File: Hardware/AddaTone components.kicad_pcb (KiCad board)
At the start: 2 copper layers, 60 x 110 mm, 95 parts, among them J1 SWD_Header, J2 Conn_01x10_Female, J3 Conn_01x12_Female, J4 Conn_01x03_Male, J5 Conn_01x06_Male, J6 Conn_01x03_Male, J7 Conn_01x02_Male, J8 Eurorack_16_pin_power, U1 STM32F446RETx, U2 ICE40UP5K-SG48ITR, U3 MCP6004, U4 PCM5100APW, U5 TL072, U6 LD1117S12TR, U7 LM1117-3.3, Y1 ECS-12MHz

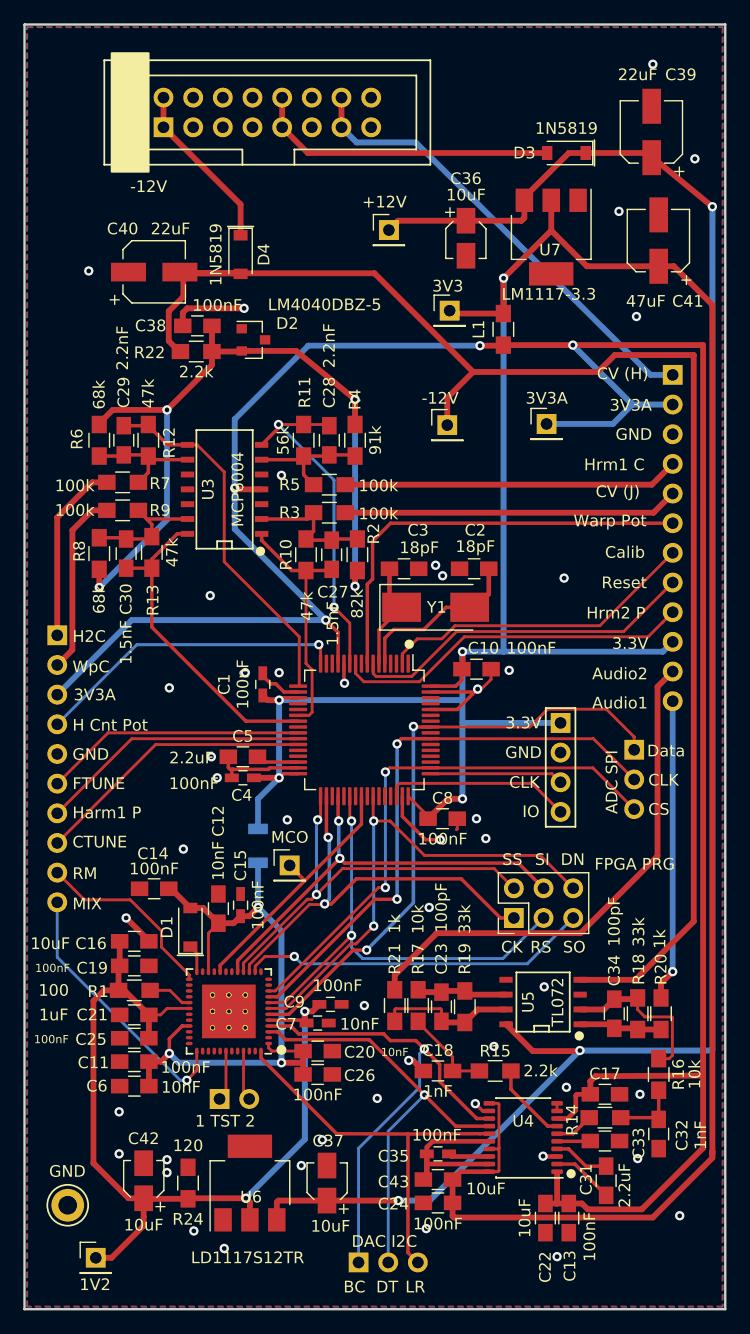
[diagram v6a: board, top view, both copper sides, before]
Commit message: Updating component schematic and PCB to Kicad 7.09
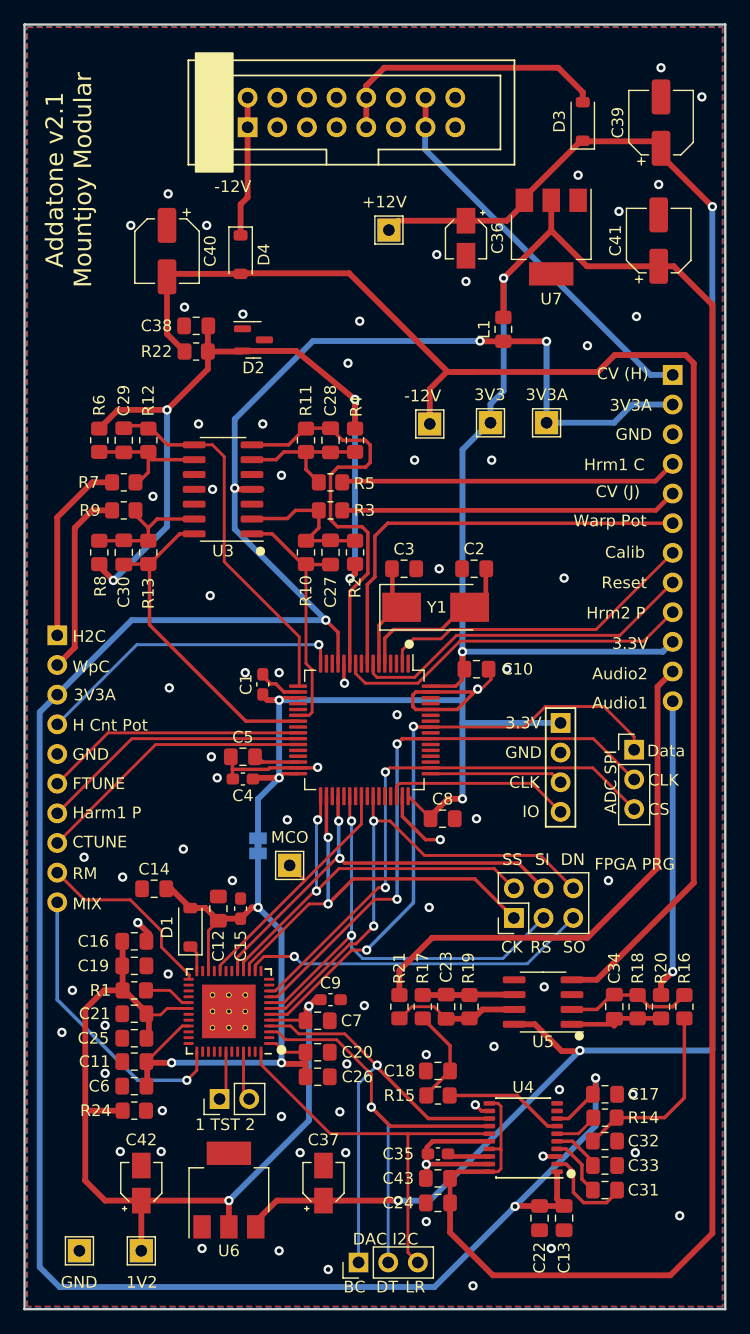
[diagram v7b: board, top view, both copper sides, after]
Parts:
- C1, C15, C35, C4, C9: footprint Capacitors_SMD:C_0603_HandSoldering -> Capacitor_SMD:C_0603_1608Metric_Pad1.08x0.95mm_HandSolder
- C10, C11, C12, C13, C14, C16, C17, C18, C19, C20, C21, C22, C23, C24, C25, C26, C27, C28, C29, C30, C31, C32, C33, C34, C38, C43, C5, C6, C8: footprint Capacitors_SMD:C_0805_HandSoldering -> Capacitor_SMD:C_0805_2012Metric_Pad1.18x1.45mm_HandSolder
- C2, C3: value 18pF -> 30pF; footprint Capacitors_SMD:C_0805_HandSoldering -> Capacitor_SMD:C_0805_2012Metric_Pad1.18x1.45mm_HandSolder
- C36, C37, C42: footprint Capacitors_SMD:CP_Elec_3x5.3 -> Capacitor_SMD:CP_Elec_3x5.3
- C39, C40, C41: footprint Capacitors_SMD:CP_Elec_5x5.3 -> Capacitor_SMD:CP_Elec_5x5.3
- C7: footprint Capacitors_SMD:C_0603_HandSoldering -> Capacitor_SMD:C_0805_2012Metric_Pad1.18x1.45mm_HandSolder
- D1, D3, D4: footprint Diodes_SMD:D_SOD-123 -> Diode_SMD:D_SOD-123
- D2: footprint TO_SOT_Packages_SMD:SOT-23 -> Package_TO_SOT_SMD:SOT-23
- J2: footprint Socket_Strips:Socket_Strip_Straight_1x10_Pitch2.54mm -> Connector_PinSocket_2.54mm:PinSocket_1x10_P2.54mm_Vertical
- J3: footprint Socket_Strips:Socket_Strip_Straight_1x12_Pitch2.54mm -> Connector_PinSocket_2.54mm:PinSocket_1x12_P2.54mm_Vertical
- J4, J6: footprint Pin_Headers:Pin_Header_Straight_1x03_Pitch2.54mm -> Connector_PinHeader_2.54mm:PinHeader_1x03_P2.54mm_Vertical
- J5: footprint Pin_Headers:Pin_Header_Straight_2x03_Pitch2.54mm -> Connector_PinHeader_2.54mm:PinHeader_2x03_P2.54mm_Vertical
- J7: footprint Pin_Headers:Pin_Header_Straight_1x02_Pitch2.54mm -> Connector_PinHeader_2.54mm:PinHeader_1x02_P2.54mm_Vertical
- L1: footprint Inductors_SMD:L_0805_HandSoldering -> Inductor_SMD:L_0805_2012Metric_Pad1.15x1.40mm_HandSolder
- R1, R10, R11, R12, R13, R14, R15, R16, R17, R18, R19, R2, R20, R21, R22, R24, R3, R4, R5, R6, R7, R8, R9: footprint Resistors_SMD:R_0805_HandSoldering -> Resistor_SMD:R_0805_2012Metric_Pad1.20x1.40mm_HandSolder
- R23: footprint Resistors_SMD:R_1206 -> Jumper:SolderJumper-2_P1.3mm_Bridged_Pad1.0x1.5mm
- TP1, TP2, TP3, TP4, TP5, TP6: footprint Pin_Headers:Pin_Header_Straight_1x01_Pitch2.54mm -> TestPoint:TestPoint_THTPad_2.0x2.0mm_Drill1.0mm
- TP7: footprint Measurement_Points:Test_Point_Keystone_5010-5014_Multipurpose -> TestPoint:TestPoint_THTPad_2.0x2.0mm_Drill1.0mm
- U3: footprint SMD_Packages:SOIC-14_N -> Package_SO:SOIC-14_3.9x8.7mm_P1.27mm
- U5: footprint SMD_Packages:SOIC-8-N -> Package_SO:SOIC-8_3.9x4.9mm_P1.27mm
- U6, U7: footprint TO_SOT_Packages_SMD:SOT-223 -> Package_TO_SOT_SMD:SOT-223
- moved TP2 10.2 mm to (139.9, 84.1)
- moved R24 7.72 mm to (109.4, 143.0), turned to 0 degrees
- moved J8 7.20 mm to (119.1, 58.8)
- moved R16 6.20 mm to (156.5, 134.1)
- moved R15 5.33 mm to (135.4, 141.7)
- moved C32 4.64 mm to (149.7, 145.6), turned to 180 degrees
- moved TP7 4.03 mm to (104.7, 155.0)
- moved TP3 3.95 mm to (110.0, 155.0)
- moved D3 3.04 mm to (147.8, 58.3), turned to 90 degrees
- moved C40 2.11 mm to (112.2, 69.4), turned to -90 degrees
- moved C33 2.10 mm to (149.7, 147.7)
- moved U6 1.90 mm to (117.5, 149.8)
- moved TP5 1.50 mm to (134.7, 84.2)
- moved C39 1.13 mm to (154.5, 58.4)
- moved C31 0.81 mm to (149.7, 149.8), turned to 180 degrees
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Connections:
- net ADC_CS renamed /ADC_CS
- net ADC_Clock renamed /ADC_Clock
- net ADC_Data renamed /ADC_Data
- net AREF_-5 renamed /AREF_-5
- net AUDIO1_OUT renamed /AUDIO1_OUT
- net AUDIO2_OUT renamed /AUDIO2_OUT
- net CTUNE renamed /CTUNE
- net CV_IN renamed /CV_IN
- net Calibration renamed /Calibration
- net DAC1_OUT renamed /DAC1_OUT
- net DAC2_OUT renamed /DAC2_OUT
- net DAC_BCLK renamed /DAC_BCLK
- net DAC_DATA renamed /DAC_DATA
- net DAC_LRCLK renamed /DAC_LRCLK
- net FPGA_DONE renamed /FPGA_DONE
- net FPGA_RESET renamed /FPGA_RESET
- net FPGA_SCK renamed /FPGA_SCK
- net FPGA_SI renamed /FPGA_SI
- net FPGA_SO renamed /FPGA_SO
- net FPGA_SS renamed /FPGA_SS
- net FTUNE renamed /FTUNE
- net F_TEST1 renamed /F_TEST1
- net F_TEST2 renamed /F_TEST2
- net HARM1_CV renamed /HARM1_CV
- net HARM1_CVIN renamed /HARM1_CVIN
- net HARM1_POT renamed /HARM1_POT
- net HARM2_CV renamed /HARM2_CV
- net HARM2_CVIN renamed /HARM2_CVIN
- net HARM2_POT renamed /HARM2_POT
- net HARM_COUNT_POT renamed /HARM_COUNT_POT
- net MCO2_CLOCK_OUT renamed /MCO2_CLOCK_OUT
- net MIX_SWITCH renamed /MIX_SWITCH
- net PITCH_CV renamed /PITCH_CV
- net PITCH_CVIN renamed /PITCH_CVIN
- net RESET renamed /RESET
- net RING_MOD renamed /RING_MOD
- net SWCLK renamed /SWCLK
- net SWDIO renamed /SWDIO
- net VCCIO_0 renamed /FPGA_3V3
- net WARP_CV renamed /WARP_CV
- net WARP_CVIN renamed /WARP_CVIN
- net WARP_POT renamed /WARP_POT
- J8 pad 11: Net-(J8-Pad11) -> unconnected-(J8-Pad11)
- J8 pad 12: Net-(J8-Pad12) -> unconnected-(J8-Pin_12-Pad12)
- J8 pad 15: Net-(J8-Pad15) -> unconnected-(J8-Pin_15-Pad15)
- J8 pad 16: Net-(J8-Pad16) -> unconnected-(J8-Pin_16-Pad16)
- U1 pad 1: Net-(U1-Pad1) -> unconnected-(U1-VBAT-Pad1)
- U1 pad 14: Net-(U1-Pad14) -> unconnected-(U1-PA0-Pad14)
- U1 pad 15: Net-(U1-Pad15) -> unconnected-(U1-PA1-Pad15)
- U1 pad 20: Net-(U1-Pad20) -> unconnected-(U1-PA4-Pad20)
- U1 pad 21: Net-(U1-Pad21) -> unconnected-(U1-PA5-Pad21)
- U1 pad 24: Net-(U1-Pad24) -> unconnected-(U1-PC4-Pad24)
- U1 pad 28: Net-(U1-Pad28) -> unconnected-(U1-PB2-Pad28)
- U1 pad 29: Net-(U1-Pad29) -> unconnected-(U1-PB10-Pad29)
- U1 pad 3: Net-(U1-Pad3) -> unconnected-(U1-PC14-Pad3)
- U1 pad 35: Net-(U1-Pad35) -> unconnected-(U1-PB14-Pad35)
- U1 pad 37: Net-(U1-Pad37) -> unconnected-(U1-PC6-Pad37)
- U1 pad 39: Net-(U1-Pad39) -> unconnected-(U1-PC8-Pad39)
- U1 pad 4: Net-(U1-Pad4) -> unconnected-(U1-PC15-Pad4)
- U1 pad 41: Net-(U1-Pad41) -> unconnected-(U1-PA8-Pad41)
- U1 pad 43: Net-(U1-Pad43) -> unconnected-(U1-PA10-Pad43)
- U1 pad 44: Net-(U1-Pad44) -> unconnected-(U1-PA11-Pad44)
- U1 pad 45: Net-(U1-Pad45) -> unconnected-(U1-PA12-Pad45)
- U1 pad 51: Net-(U1-Pad51) -> unconnected-(U1-PC10-Pad51)
- U1 pad 52: Net-(U1-Pad52) -> unconnected-(U1-PC11-Pad52)
- U1 pad 53: Net-(U1-Pad53) -> unconnected-(U1-PC12-Pad53)
- U1 pad 54: Net-(U1-Pad54) -> unconnected-(U1-PD2-Pad54)
- U1 pad 56: Net-(U1-Pad56) -> unconnected-(U1-PB4-Pad56)
- U1 pad 58: Net-(U1-Pad58) -> unconnected-(U1-PB6-Pad58)
- U1 pad 59: Net-(U1-Pad59) -> unconnected-(U1-PB7-Pad59)
- U1 pad 61: Net-(U1-Pad61) -> unconnected-(U1-PB8-Pad61)
- U1 pad 62: Net-(U1-Pad62) -> unconnected-(U1-PB9-Pad62)
- U1 pad 9: Net-(U1-Pad9) -> unconnected-(U1-PC1-Pad9)
- U2 pad 11: Net-(U2-Pad11) -> unconnected-(U2-IOB_20a-Pad11)
- U2 pad 12: Net-(U2-Pad12) -> unconnected-(U2-IOB_22b-Pad12)
- U2 pad 13: Net-(U2-Pad13) -> unconnected-(U2-IOB_24a-Pad13)
- U2 pad 18: Net-(U2-Pad18) -> unconnected-(U2-IOB_31b-Pad18)
- U2 pad 19: Net-(U2-Pad19) -> unconnected-(U2-IOB_29b-Pad19)
- U2 pad 2: Net-(U2-Pad2) -> unconnected-(U2-IOB_6a-Pad2)
- U2 pad 21: Net-(U2-Pad21) -> unconnected-(U2-IOB_23b-Pad21)
- U2 pad 23: Net-(U2-Pad23) -> unconnected-(U2-IOT_37a-Pad23)
- U2 pad 26: Net-(U2-Pad26) -> unconnected-(U2-IOT_39a-Pad26)
- U2 pad 27: Net-(U2-Pad27) -> unconnected-(U2-IOT_38b-Pad27)
- U2 pad 28: Net-(U2-Pad28) -> unconnected-(U2-IOT_41a-Pad28)
- U2 pad 31: Net-(U2-Pad31) -> unconnected-(U2-IOT_42b-Pad31)
- U2 pad 32: Net-(U2-Pad32) -> unconnected-(U2-IOT_43a-Pad32)
- U2 pad 34: Net-(U2-Pad34) -> unconnected-(U2-IOT_44b-Pad34)
- U2 pad 35: Net-(U2-Pad35) -> unconnected-(U2-IOT_46b_G0-Pad35)
- U2 pad 36: Net-(U2-Pad36) -> unconnected-(U2-IOT_48b-Pad36)
- U2 pad 38: Net-(U2-Pad38) -> unconnected-(U2-IOT_50b-Pad38)
- U2 pad 39: Net-(U2-Pad39) -> unconnected-(U2-RGB0-Pad39)
- U2 pad 40: Net-(U2-Pad40) -> unconnected-(U2-RGB1-Pad40)
- U2 pad 41: Net-(U2-Pad41) -> unconnected-(U2-RGB2-Pad41)
- U2 pad 43: Net-(U2-Pad43) -> unconnected-(U2-IOT_49a-Pad43)
- U2 pad 44: Net-(U2-Pad44) -> unconnected-(U2-IOB_3b_G6-Pad44)
- U2 pad 46: Net-(U2-Pad46) -> unconnected-(U2-IOB_0a-Pad46)
- U2 pad 47: Net-(U2-Pad47) -> unconnected-(U2-IOB_2a-Pad47)
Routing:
- net Net-(C32-Pad2): track 5.81 -> 16.2 mm
- net +3V3: track 263.3 -> 271.1 mm
- net /HARM1_CV: track 29.7 -> 36.0 mm, vias 2 -> 0
- net /CV_IN: track 39.6 -> 33.7 mm
- net GND: track 59.8 -> 54.8 mm, vias 47 -> 76
- net /DAC_BCLK: track 43.7 -> 39.9 mm
- net VEE: track 126.2 -> 122.4 mm
- net /DAC2_OUT: track 6.83 -> 10.3 mm
- net +3.3VA: track 217.3 -> 220.5 mm, vias 4 -> 6
- net Net-(U5A--): track 14.1 -> 11.0 mm
- net Net-(U4-CAPP): track 5.31 -> 8.10 mm
- net -12V: track 14.5 -> 12.0 mm
- net /MIX_SWITCH: track 23.0 -> 25.2 mm
- net /FPGA_3V3: track 57.0 -> 58.9 mm
- net +12V: track 26.1 -> 24.5 mm
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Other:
- board text added: "Addatone v2.1 Mountjoy Modular"
- board text removed: "Addatone v2.0 Mountjoy Modular"

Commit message: Updated schematic and pcb to v2.1
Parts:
- removed R23: 0, Jumper:SolderJumper-2_P1.3mm_Bridged_Pad1.0x1.5mm
- added JP1: Jumper_2_Bridged, Jumper:SolderJumper-2_P1.3mm_Bridged_Pad1.0x1.5mm, B.Cu at (120.0, 120.3)
- moved L1 4.12 mm to (145.1, 75.7), turned to 180 degrees
- moved C39 0.20 mm to (154.3, 58.4)
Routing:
- net VEE: track 122.4 -> 129.0 mm
- net +3.3VA: track 220.5 -> 225.6 mm, vias 6 -> 4
- net +3V3: track 271.1 -> 272.8 mm, vias 5 -> 4
- net +1V2: track 79.2 -> 80.2 mm
- net /RING_MOD: track 16.1 -> 16.6 mm
- net GND: track 54.8 -> 54.7 mm, vias 76 -> 75
